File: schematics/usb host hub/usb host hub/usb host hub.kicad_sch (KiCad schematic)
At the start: 48 parts, among them J1 USB_A, J2 USB_A, J3 USB_A, J4 Conn_01x04_Male, J5 532610671, U1 RP2040, U2 FE1.1s, U3 W25Q128JVS, U4 AZ1117EH-3.3TRG1, U5 USBLC6-2SC6, U6 USBLC6-2SC6, U7 USBLC6-2SC6, Y1 12MHz, Y2 12MHz

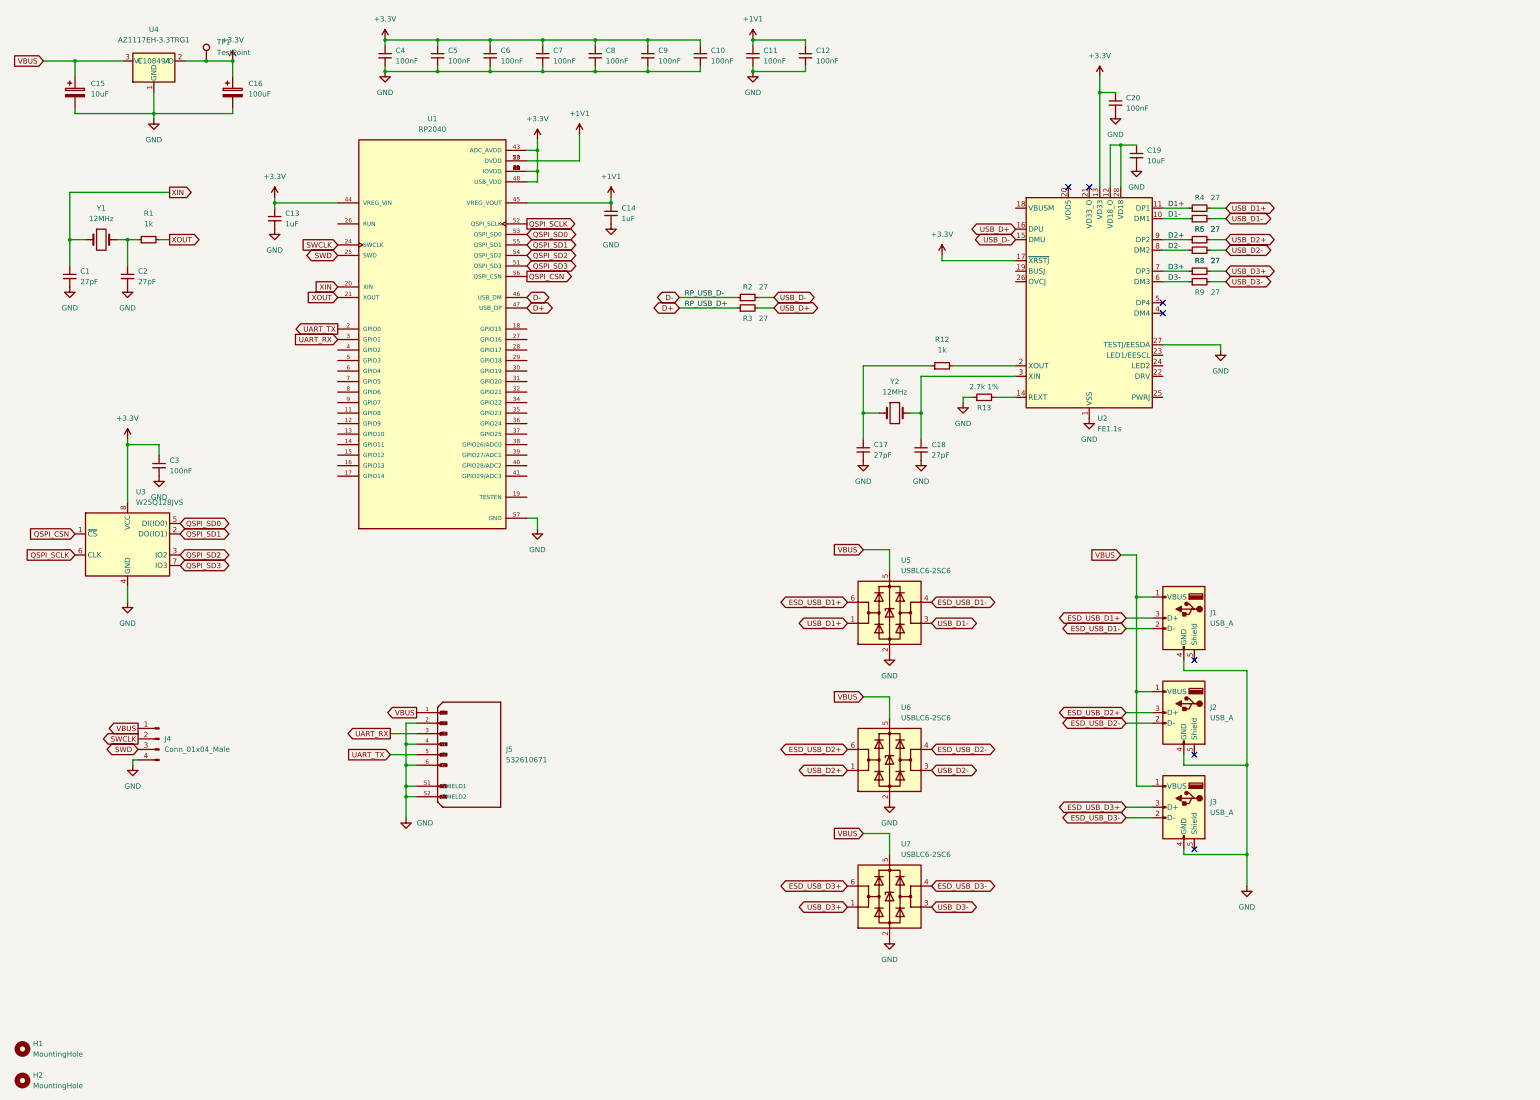
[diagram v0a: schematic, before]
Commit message: Rv32: USB host schematic updated.
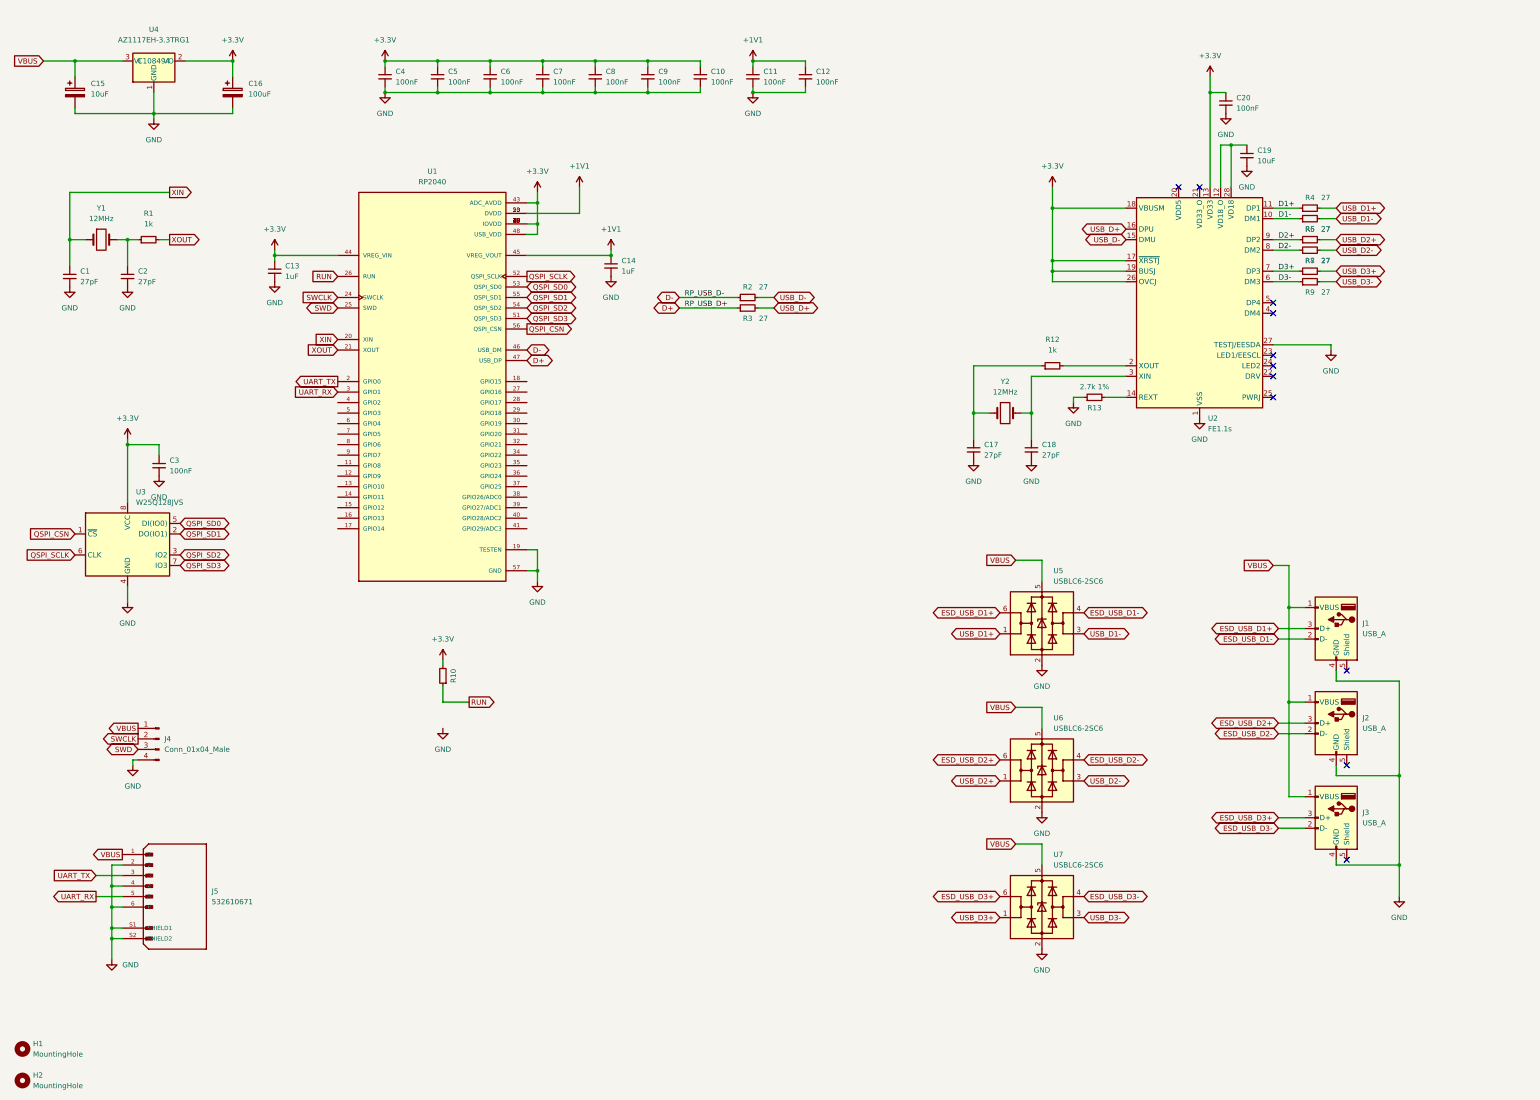
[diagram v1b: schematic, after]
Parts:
- removed TP1: TestPoint, TestPoint:TestPoint_Pad_D1.5mm, symbol Connector:TestPoint
- added R10: (no value), symbol Device:R_Small
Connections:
- net +3V3: now also U2.18 (VBUSM), U2.19 (BUSJ), U2.26 (OVCJ), R10.2
- net GND: now also U1.19 (TESTEN)
- net UART_RX: now also J5.5; no longer J5.3
- net UART_TX: now also J5.3; no longer J5.5
- net RUN: now reaches U1.26 (RUN)
- net RUN: now also R10.1
- no-connect marks 7 -> 11
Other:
- moved on the sheet: C10, C11, C12, C13, C14, C17, C18, C19, C20, C4, C5, C6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

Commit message: Rv32: Some work on USB HID board.
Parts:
- removed J5: 532610671, MOLEX_532610671, symbol 532610671:532610671
- added J5: (no value), symbol Connector:Conn_01x04_Male
- J1: value USB_A -> (none); footprint Connector_USB:USB_A_TE_292303-7_Horizontal -> (none)
- U1: value RP2040 -> (none); footprint QFN40P700X700X90-57N -> (none); LCSC (none) -> C2040
- U2: value FE1.1s -> (none); footprint Package_SO:SSOP-28_3.9x9.9mm_P0.635mm -> (none); LCSC (none) -> C9359
- U3: value W25Q128JVS -> (none); footprint Package_SO:SOIC-8_5.23x5.23mm_P1.27mm -> (none); LCSC (none) -> C97521
- U4: value AZ1117EH-3.3TRG1 -> (none); footprint Package_TO_SOT_SMD:SOT-223-3_TabPin2 -> (none)
- U5, U6, U7: value USBLC6-2SC6 -> (none); footprint Package_TO_SOT_SMD:SOT-23-6 -> (none)
- Y1, Y2: value 12MHz -> (none); footprint Crystal:Crystal_SMD_HC49-SD -> (none)
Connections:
- net GND: now also J5.1 (Pin_1)
- net SWCLK: now also J4.3 (Pin_3); no longer J4.2 (Pin_2)
- net SWD: now also J4.2 (Pin_2); no longer J4.3 (Pin_3)
- net UART_RX: now also J5.3 (Pin_3)
- net UART_TX: now also J5.2 (Pin_2)
- net VBUS: now also J5.4 (Pin_4)
- net VD18: now reaches C19.1, U2.12 (VD18_O), U2.28 (VD18)

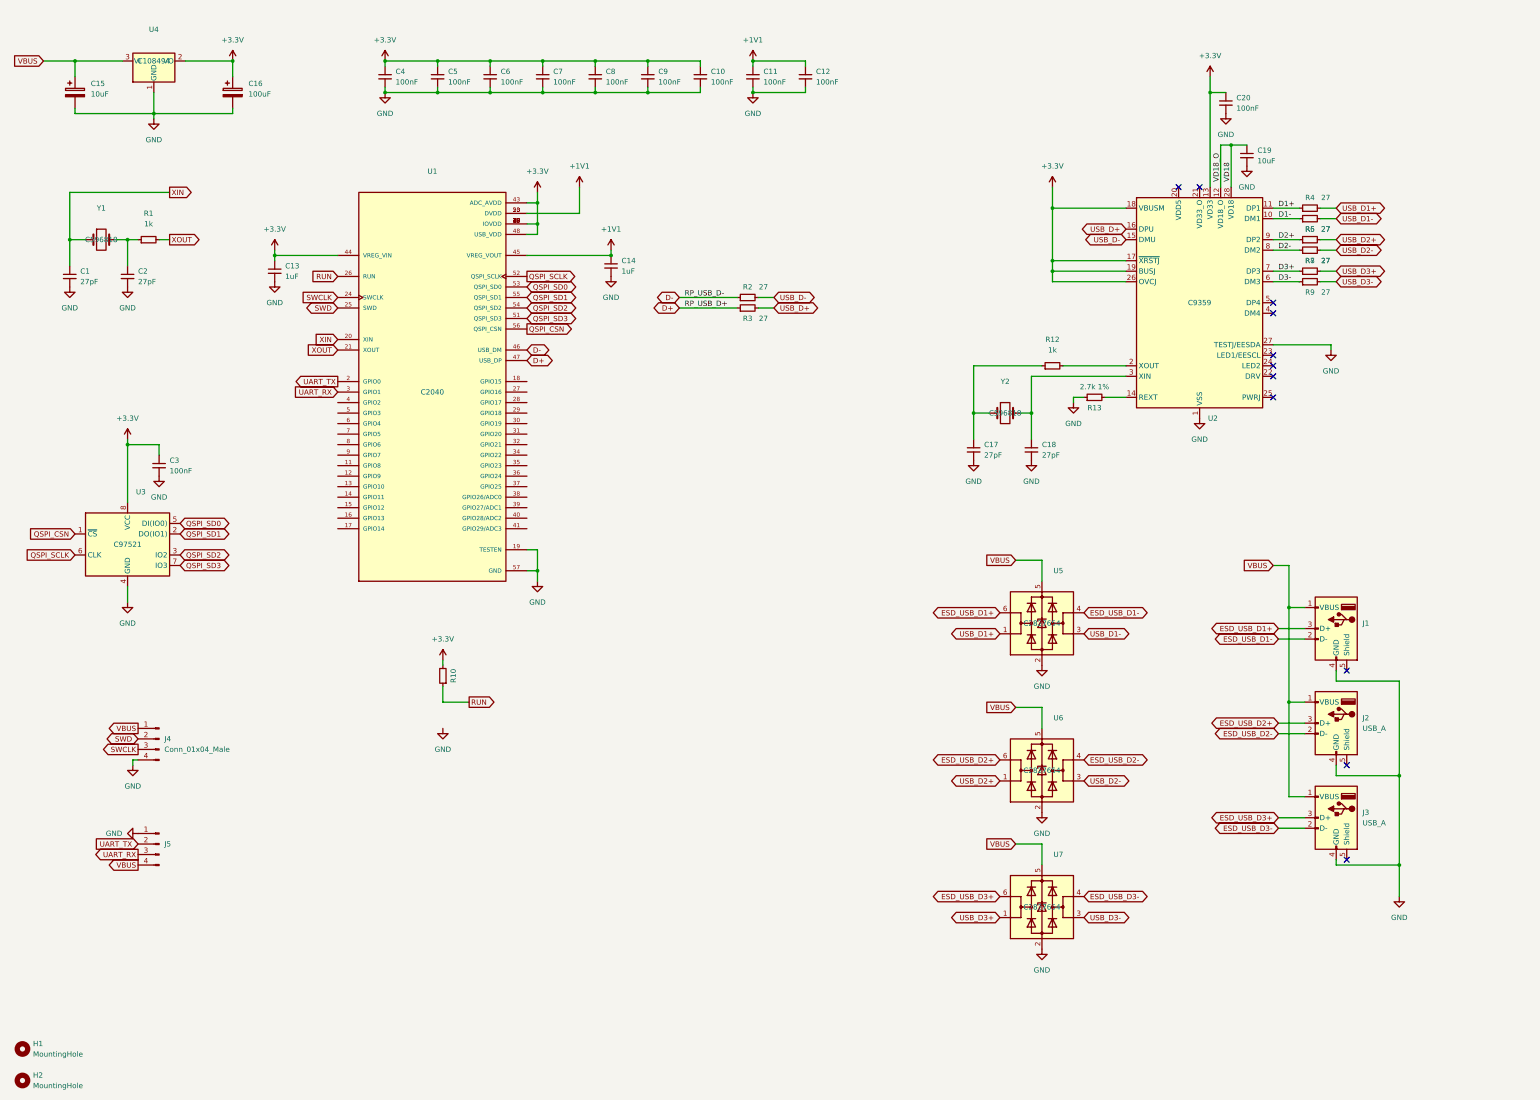
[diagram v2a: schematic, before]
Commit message: Rv32: More USB host board work, using USB connector available on JLCPCB.
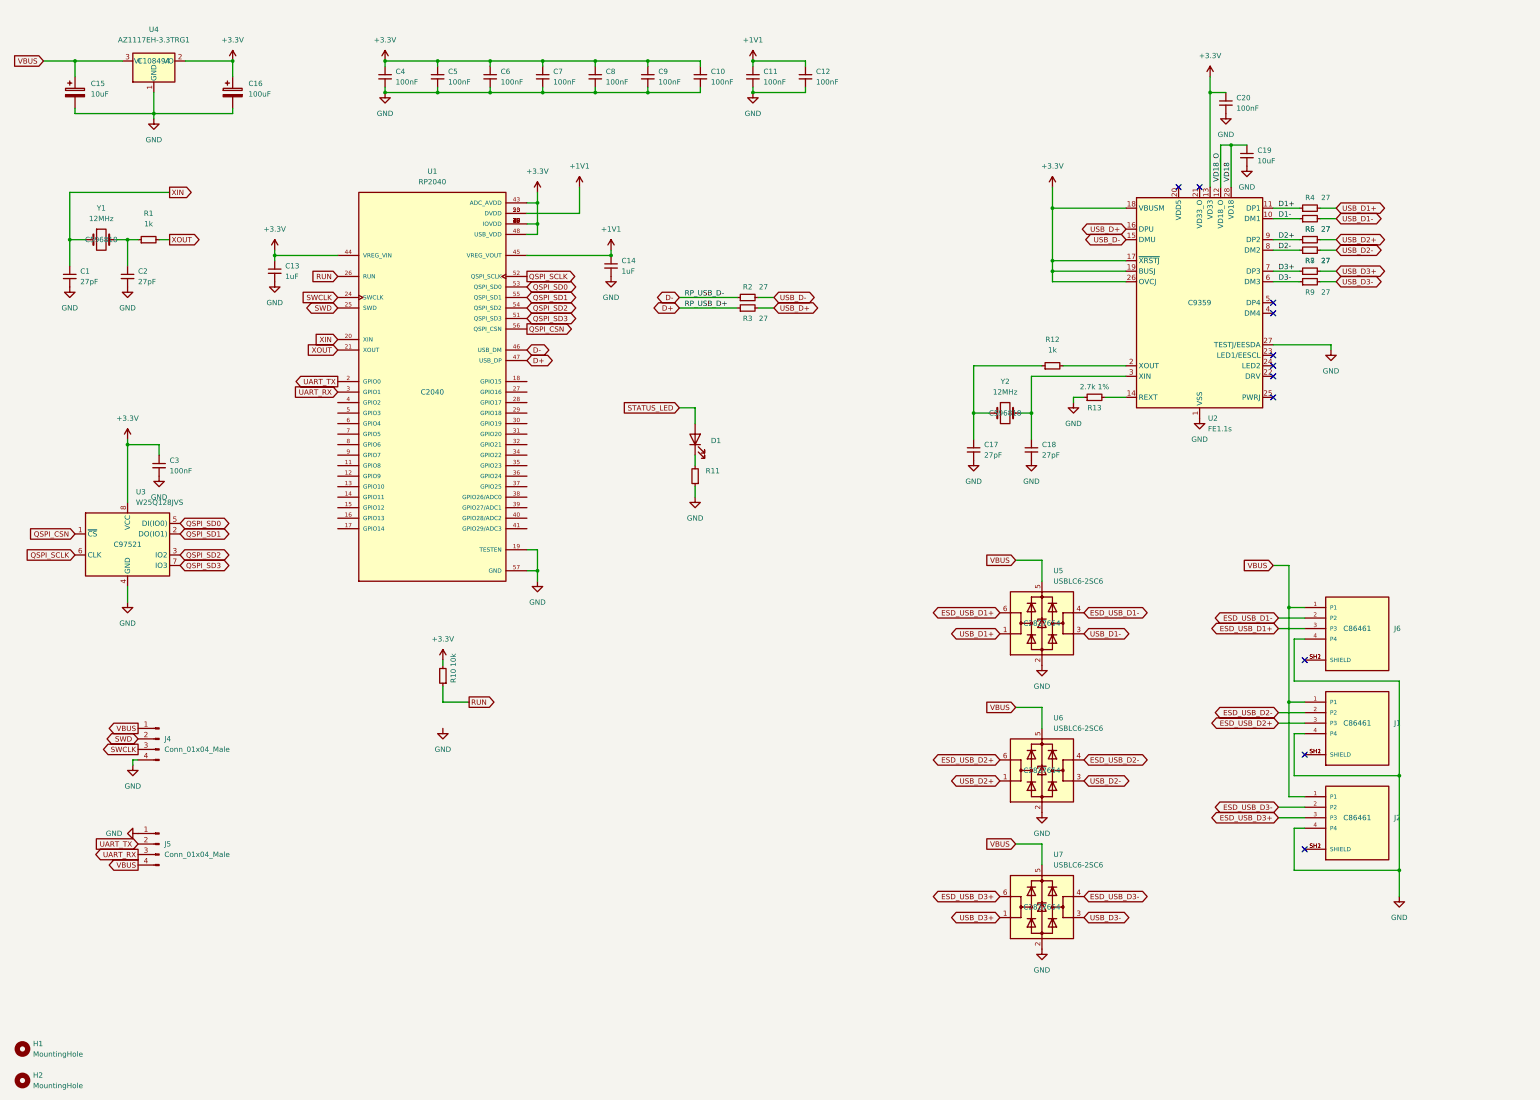
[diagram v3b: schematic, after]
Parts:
- removed J1: (no value), symbol Connector:USB_A
- removed J2, J3: USB_A, Connector_USB:USB_A_TE_292303-7_Horizontal, symbol Connector:USB_A
- added D1: (no value), symbol Device:LED
- added J1, J2, J6: (no value), symbol 292303-1:292303-1
- added R11: (no value), symbol Device:R_Small
- J5: value (none) -> Conn_01x04_Male; footprint (none) -> Connector_JST:JST_EH_B4B-EH-A_1x04_P2.50mm_Vertical
- R10: value (none) -> 10k; footprint (none) -> Resistor_SMD:R_0402_1005Metric
- U1: value (none) -> RP2040; footprint (none) -> QFN40P700X700X90-57N
- U2: value (none) -> FE1.1s; footprint (none) -> Package_SO:SSOP-28_3.9x9.9mm_P0.635mm
- U3: value (none) -> W25Q128JVS; footprint (none) -> Package_SO:SOIC-8_5.23x5.23mm_P1.27mm
- U4: value (none) -> AZ1117EH-3.3TRG1; footprint (none) -> Package_TO_SOT_SMD:SOT-223-3_TabPin2
- U5, U6, U7: value (none) -> USBLC6-2SC6; footprint (none) -> Package_TO_SOT_SMD:SOT-23-6
- Y1, Y2: value (none) -> 12MHz; footprint (none) -> Crystal:Crystal_SMD_HC49-SD
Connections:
- net ESD_USB_D1+: now also J6.3 (P3)
- net ESD_USB_D1-: now also J6.2 (P2)
- net ESD_USB_D2+: now also J1.3 (P3)
- net ESD_USB_D2-: now also J1.2 (P2)
- net ESD_USB_D3+: now also J2.3 (P3)
- net ESD_USB_D3-: now also J2.2 (P2)
- net GND: now also J1.4 (P4), J2.4 (P4), J6.4 (P4), R11.1
- net VBUS: now also J1.1 (P1), J2.1 (P1), J6.1 (P1)
- new net: J1.SH1 (SHIELD), J1.SH2 (SHIELD)
- new net: J6.SH1 (SHIELD), J6.SH2 (SHIELD)
- new net: J2.SH1 (SHIELD), J2.SH2 (SHIELD)
- new net: D1.1 (K), R11.2
- new net STATUS_LED: D1.2 (A)

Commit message: Rv32: USB HID HUB schematic updated. Ordered from JLCPCB.
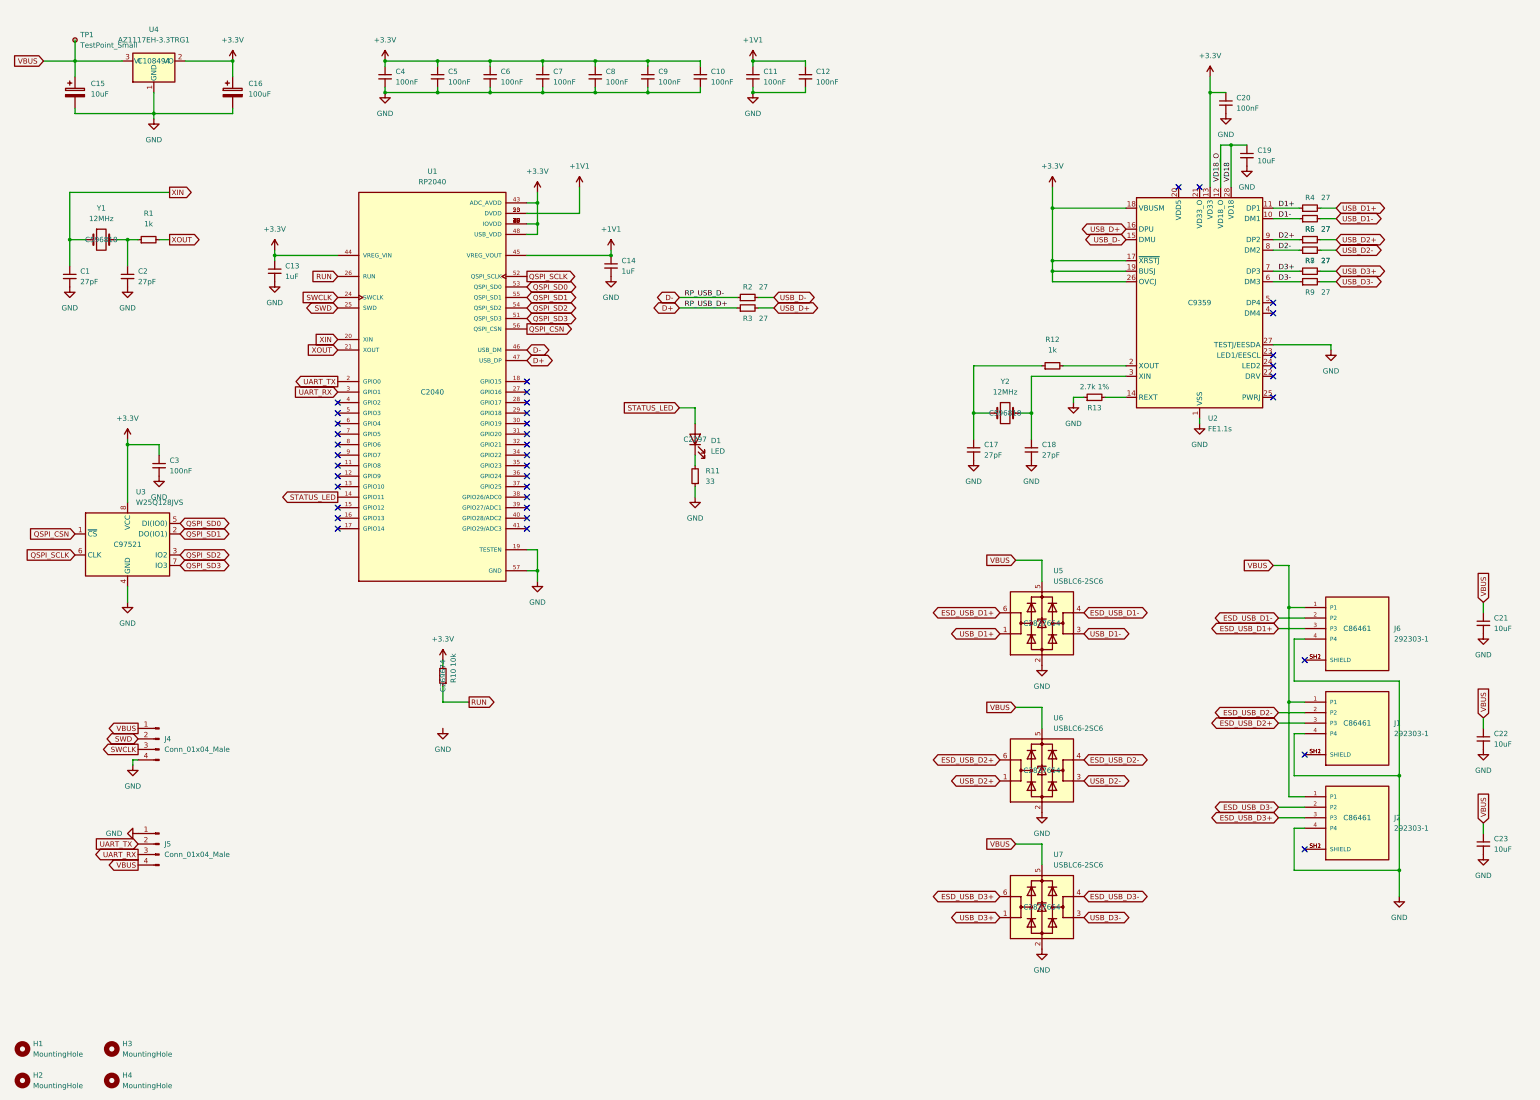
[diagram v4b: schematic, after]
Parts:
- added C21, C22, C23: 10uF, Capacitor_SMD:C_0805_2012Metric, symbol Device:C_Small
- added H3, H4: MountingHole, MountingHole:MountingHole_3.2mm_M3_DIN965_Pad, symbol Mechanical:MountingHole
- added TP1: TestPoint_Small, TestPoint:TestPoint_Pad_D1.5mm, symbol Connector:TestPoint_Small
- C10, C11, C12, C20, C3, C4, C5, C6, C7, C8, C9: LCSC (none) -> C307331
- D1: value (none) -> LED; footprint (none) -> LED_SMD:LED_0805_2012Metric; LCSC (none) -> C2297
- J1, J2, J6: value (none) -> 292303-1; footprint (none) -> 292303-1:TE_292303-1
- R10: LCSC (none) -> C269674
- R11: value (none) -> 33; footprint (none) -> Resistor_SMD:R_0805_2012Metric
- R13: LCSC (none) -> C25885
- U1: footprint QFN40P700X700X90-57N -> parts:QFN40P700X700X90-57N
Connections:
- net GND: now also C21.2, C22.2, C23.2
- net STATUS_LED: now also U1.14 (GPIO11)
- net VBUS: now also C21.1, C22.1, C23.1, TP1.1
- no-connect marks 11 -> 38
